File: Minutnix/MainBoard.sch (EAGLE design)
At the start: 120 parts, among them IC3 TP4056, IC7 FT232RL, Q4 32.768kHz, X1 FH12-12S-0.5S_THINNER, X2 JST-XH-03-PIN-LONG-PAD, X4 JST-XH-03-PIN-LONG-PAD

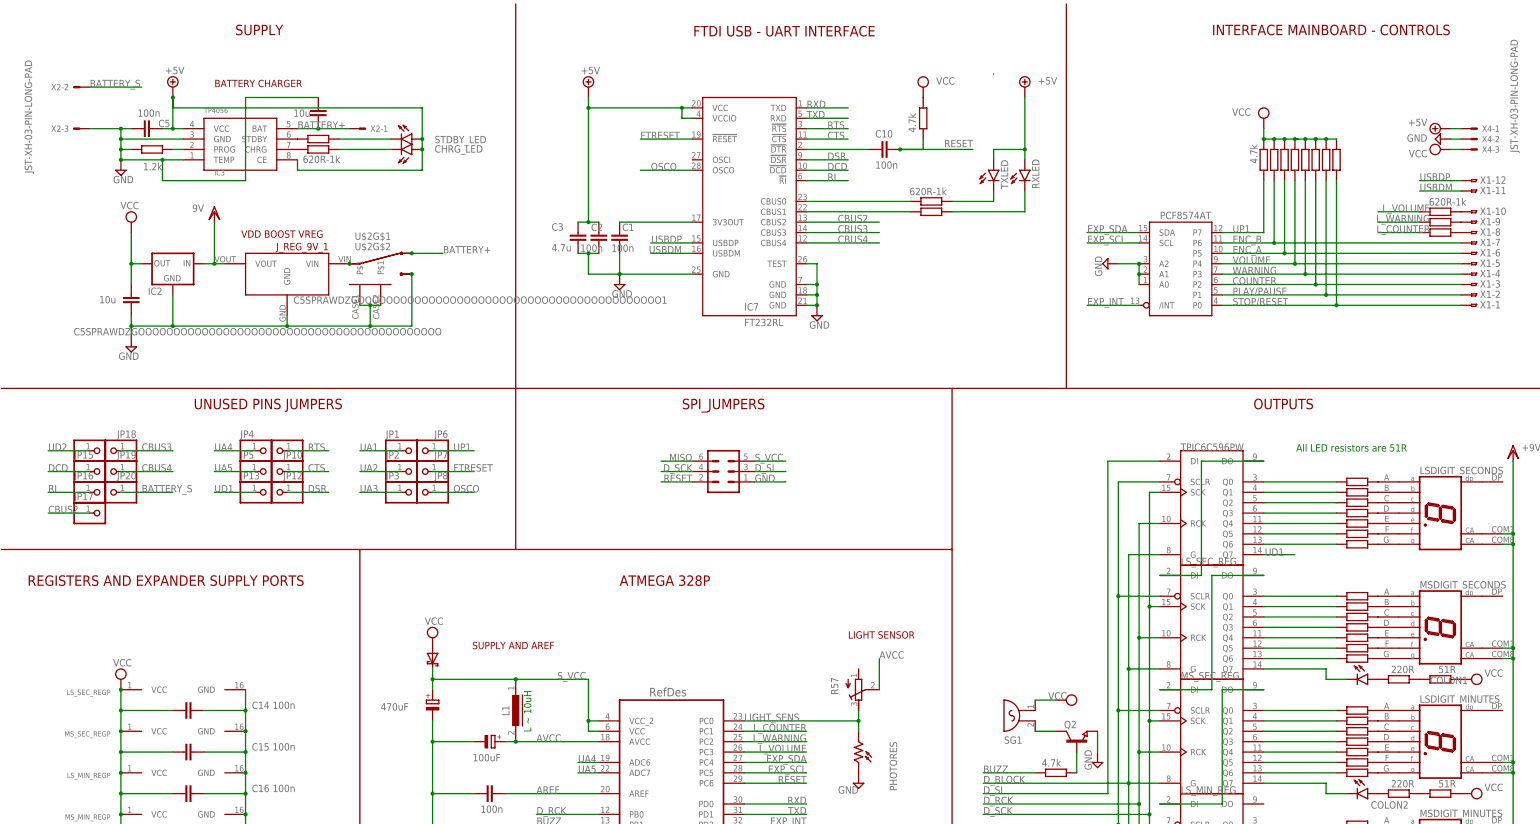
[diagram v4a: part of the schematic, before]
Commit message: Final packages
+most paths wider (24 mils)
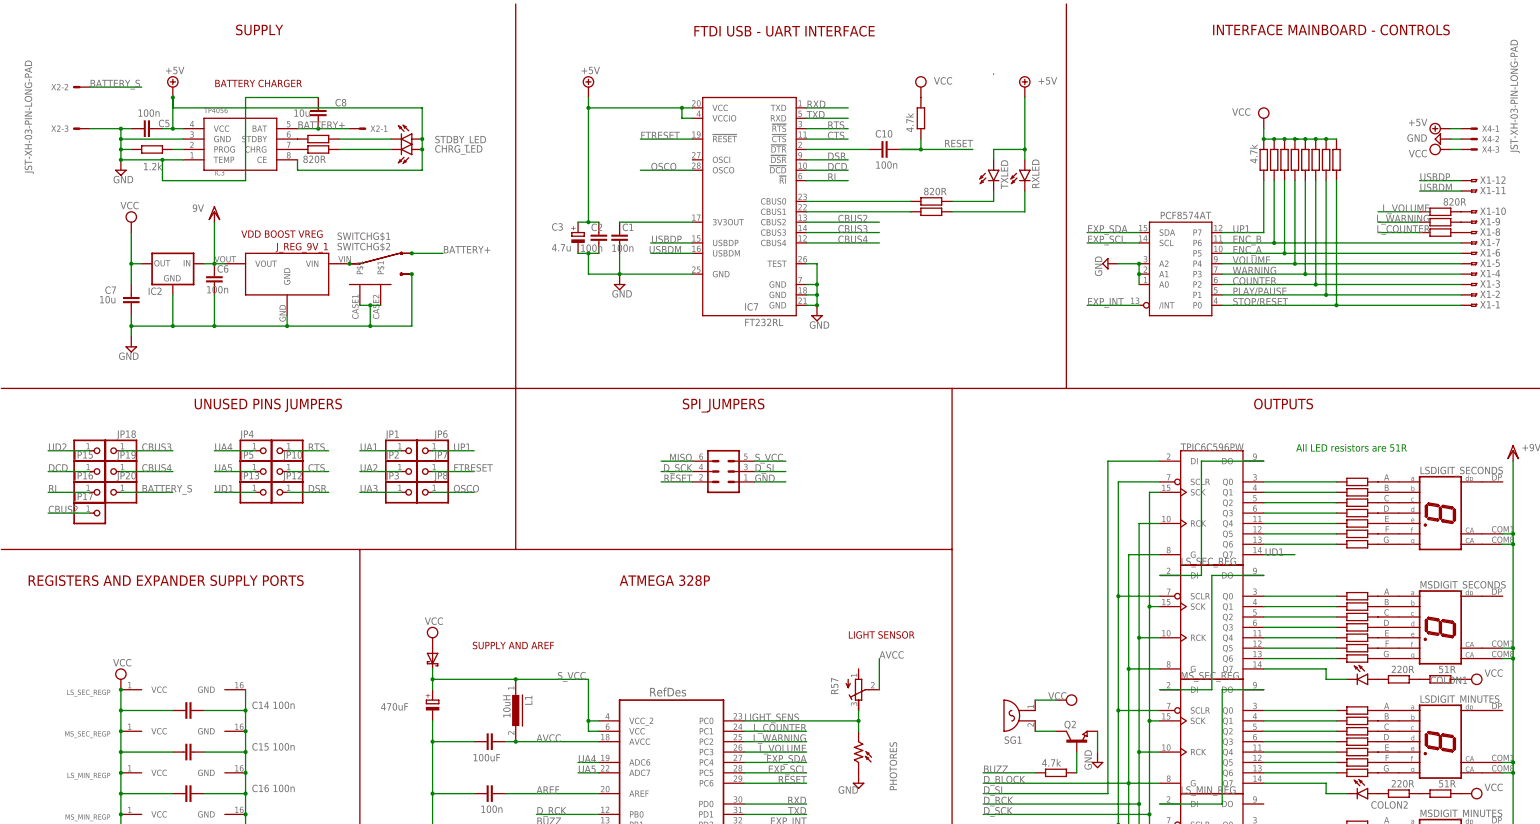
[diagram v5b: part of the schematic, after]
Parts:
- removed C5SPRAWDZGOOOOOOOOOOOOOOOOOOOOOOOOOOOOOOOOOOOOOOOOOOO, C5SPRAWDZGOOOOOOOOOOOOOOOOOOOOOOOOOOOOOOOOOOOOOOOOOOO1: 10u, rcl:C-EUC3216
- added C6: 100n, rcl:C-EUC0603
- added C7, C8: 10u, rcl:C-EUC1206
- C3: device rcl:C-EUC3216 -> rcl:CPOL-EUSMCB
- C32: device rcl:CPOL-EU140CLH-1010 -> rcl:C-EUC1210
- R39, R40, R47, R52, R64, R65, R66: value 620R-1k -> 820R
- renumbered U$2 to SWITCH
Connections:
- net +5V: now also C3.+; no longer C3.1
- net AVCC: now also C32.1; no longer C32.+
- net BATTERY+: now also C8.2; no longer C5SPRAWDZGOOOOOOOOOOOOOOOOOOOOOOOOOOOOOOOOOOOOOOOOOOO1.2
- net GND: now also C3.-, C32.2, C6.1, C7.2, C8.1; no longer C3.2, C32.-, C5SPRAWDZGOOOOOOOOOOOOOOOOOOOOOOOOOOOOOOOOOOOOOOOOOOO.2, C5SPRAWDZGOOOOOOOOOOOOOOOOOOOOOOOOOOOOOOOOOOOOOOOOOOO1.1
- net VCC: now also C7.1; no longer C5SPRAWDZGOOOOOOOOOOOOOOOOOOOOOOOOOOOOOOOOOOOOOOOOOOO.1
- net VDD: now also C6.2
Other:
- note removed: "L ~ 10uH"

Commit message: Mixing led signals
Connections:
- net N$10 renamed LS_F
- net N$62 renamed MS_F
- net N$72 renamed LM_F
- net N$95 renamed MM_F
- removed net N$11: LS_SEC_REGG$1.Q6, R15.2
- removed net N$2: COLON1.C, MS_SEC_REGG$1.Q7
- removed net N$20: COLON2.C, LS_MIN_REGG$1.Q7
- removed net N$22: MS_MIN_REGG$1.Q0, R27.2
- removed net N$4: MS_SEC_REGG$1.Q0, R14.2
- removed net N$5: LS_SEC_REGG$1.Q0, R21.2
- removed net N$58: MS_SEC_REGG$1.Q1, R13.2
- removed net N$59: MS_SEC_REGG$1.Q2, R12.2
- removed net N$6: LS_SEC_REGG$1.Q1, R20.2
- removed net N$60: MS_SEC_REGG$1.Q3, R11.2
- removed net N$61: MS_SEC_REGG$1.Q4, R10.2
- removed net N$63: MS_SEC_REGG$1.Q6, R8.2
- removed net N$67: LS_MIN_REGG$1.Q0, R7.2
- removed net N$68: LS_MIN_REGG$1.Q1, R6.2
- removed net N$69: LS_MIN_REGG$1.Q2, R5.2
- removed net N$7: LS_SEC_REGG$1.Q2, R19.2
- removed net N$70: LS_MIN_REGG$1.Q3, R4.2
- removed net N$71: LS_MIN_REGG$1.Q4, R3.2
- removed net N$73: LS_MIN_REGG$1.Q6, R1.2
- removed net N$75: MS_MIN_REGG$1.Q1, R26.2
- removed net N$76: MS_MIN_REGG$1.Q2, R25.2
- removed net N$77: MS_MIN_REGG$1.Q3, R24.2
- removed net N$8: LS_SEC_REGG$1.Q3, R18.2
- removed net N$9: LS_SEC_REGG$1.Q4, R17.2
- removed net N$94: MS_MIN_REGG$1.Q4, R23.2
- removed net N$96: MS_MIN_REGG$1.Q6, R28.2
- new net COL_1: COLON1.C, MS_SEC_REGG$1.Q0
- new net COL_2: COLON2.C, LS_MIN_REGG$1.Q0
- new net LM_A: LS_MIN_REGG$1.Q6, R7.2
- new net LM_B: LS_MIN_REGG$1.Q7, R6.2
- new net LM_C: LS_MIN_REGG$1.Q1, R5.2
- new net LM_D: LS_MIN_REGG$1.Q2, R4.2
- new net LM_E: LS_MIN_REGG$1.Q3, R3.2
- new net LM_G: LS_MIN_REGG$1.Q4, R1.2
- new net LS_A: LS_SEC_REGG$1.Q6, R21.2
- new net LS_B: LS_SEC_REGG$1.Q7, R20.2
- new net LS_C: LS_SEC_REGG$1.Q1, R19.2
- new net LS_D: LS_SEC_REGG$1.Q2, R18.2
- new net LS_E: LS_SEC_REGG$1.Q3, R17.2
- new net LS_G: LS_SEC_REGG$1.Q4, R15.2
- new net MM_A: MS_MIN_REGG$1.Q6, R27.2
- new net MM_B: MS_MIN_REGG$1.Q7, R26.2
- new net MM_C: MS_MIN_REGG$1.Q1, R25.2
- new net MM_D: MS_MIN_REGG$1.Q2, R24.2
- new net MM_E: MS_MIN_REGG$1.Q3, R23.2
- new net MM_G: MS_MIN_REGG$1.Q4, R28.2
- new net MS_A: MS_SEC_REGG$1.Q6, R14.2
- new net MS_B: MS_SEC_REGG$1.Q7, R13.2
- new net MS_C: MS_SEC_REGG$1.Q1, R12.2
- new net MS_D: MS_SEC_REGG$1.Q2, R11.2
- new net MS_E: MS_SEC_REGG$1.Q3, R10.2
- new net MS_G: MS_SEC_REGG$1.Q4, R8.2
- net UD1: now also LS_SEC_REGG$1.Q0; no longer LS_SEC_REGG$1.Q7
- net UD2: now also MS_MIN_REGG$1.Q0; no longer MS_MIN_REGG$1.Q7
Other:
- moved on the sheet: C8, COLON1, COLON2, LSDIGIT_MINUTES, LSDIGIT_SECONDS, MSDIGIT_MINUTES, MSDIGIT_SECONDS

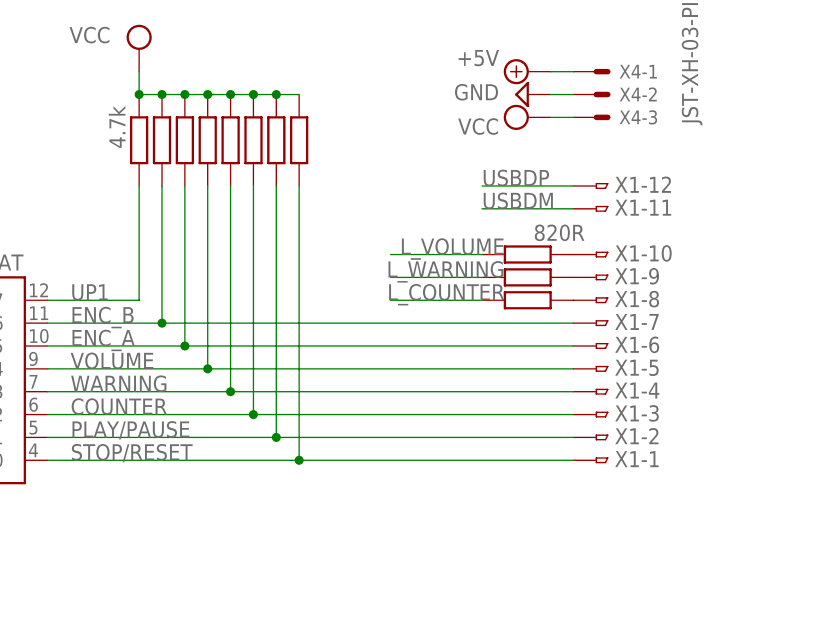
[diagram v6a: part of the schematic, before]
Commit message: rotation of tape ports
also some nets wider
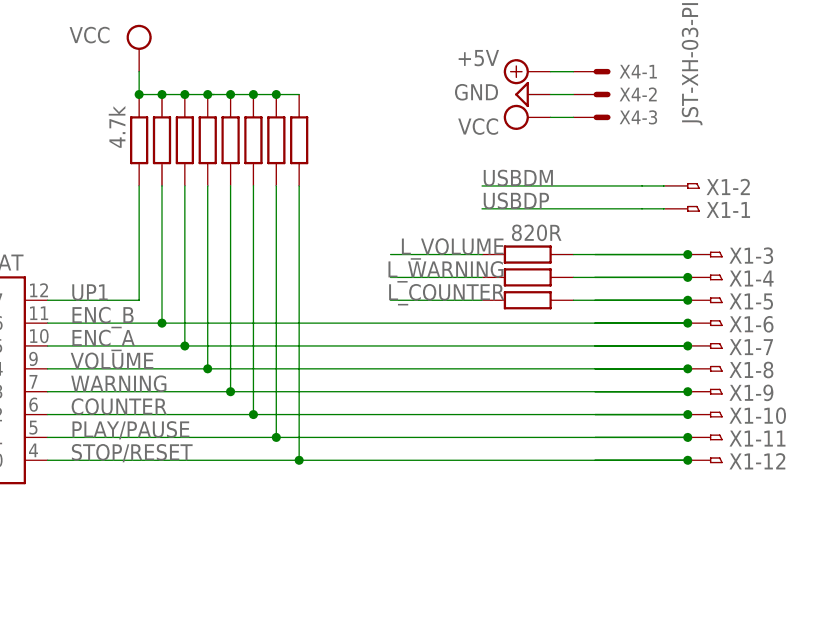
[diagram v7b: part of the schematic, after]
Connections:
- removed net N$12: R64.1, X1-10.1
- removed net N$26: R47.1, X1-9.1
- removed net N$28: R52.1, X1-8.1
- new net N$20: R64.1, X1-3.1
- new net N$22: R47.1, X1-4.1
- new net N$30: R52.1, X1-5.1
- net COUNTER: now also X1-10.1; no longer X1-3.1
- net ENC_A: now also X1-7.1; no longer X1-6.1
- net ENC_B: now also X1-6.1; no longer X1-7.1
- net PLAY/PAUSE: now also X1-11.1; no longer X1-2.1
- net STOP/RESET: now also X1-12.1; no longer X1-1.1
- net USBDM: now also X1-2.1; no longer X1-11.1
- net USBDP: now also X1-1.1; no longer X1-12.1
- net VOLUME: now also X1-8.1; no longer X1-5.1
- net WARNING: now also X1-9.1; no longer X1-4.1
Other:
- moved on the sheet: X1-1, X1-10, X1-11, X1-12, X1-2, X1-3, X1-4, X1-5, X1-6, X1-7, X1-8, X1-9

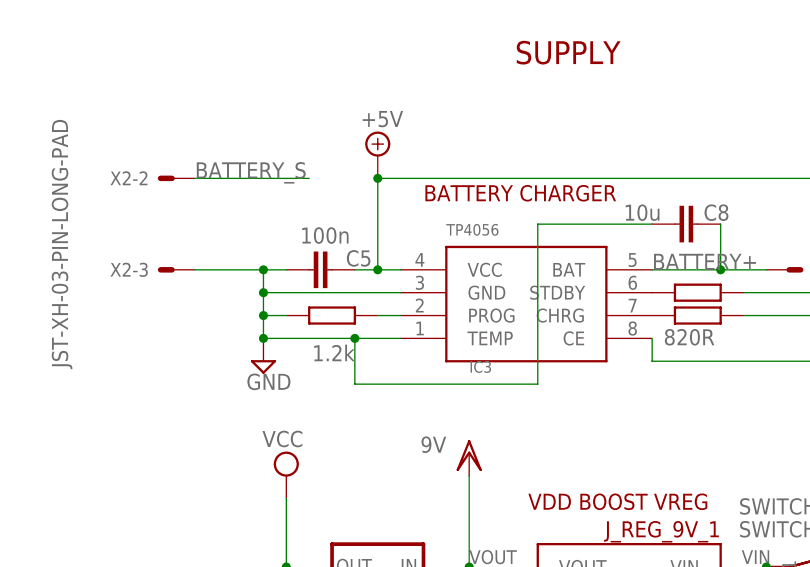
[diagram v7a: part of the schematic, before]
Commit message: Almost complete
Added 3d extraction
wider better paths
corrected Temperature field of TP to be GND
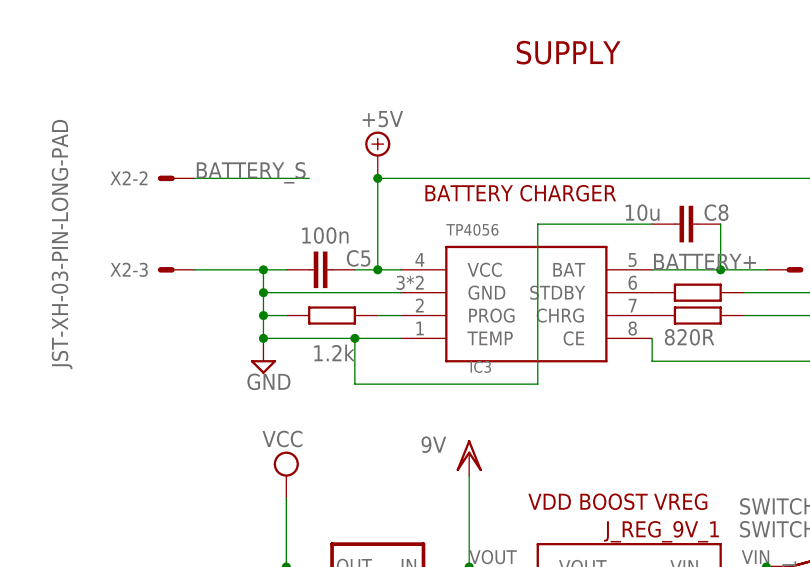
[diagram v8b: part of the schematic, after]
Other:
- moved on the sheet: IC3
